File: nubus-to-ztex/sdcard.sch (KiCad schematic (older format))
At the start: 3 parts, among them J6 47219-2001

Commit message: forgot to commit last attempt at V1.2
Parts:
- J2: renamed from J6; URL (none) -> https://eu.mouser.com/ProductDetail/Molex/47219-2001?qs=6kT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
- renumbered C16 to C10
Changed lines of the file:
@@
 $Descr A4 11693 8268
 encoding utf-8
-Sheet 6 7
+Sheet 8 9
 Title "sbus-to-ztex sdcard"
 Date ""
@@
 $EndDescr
 $Comp
-L power:GND #PWR0176
+L power:GND #PWR0124
 U 1 1 58DA7C71
 P 5450 5450
-F 0 "#PWR0176" H 5450 5200 50  0001 C CNN
+F 0 "#PWR0124" H 5450 5200 50  0001 C CNN
 F 1 "GND" H 5450 5300 50  0000 C CNN
 F 2 "" H 5450 5450 50  0000 C CNN
@@
 $EndComp
 $Comp
-L power:+3V3 #PWR0177
+L power:+3V3 #PWR0125
 U 1 1 58DA7C72
 P 5450 4600
-F 0 "#PWR0177" H 5450 4450 50  0001 C CNN
+F 0 "#PWR0125" H 5450 4450 50  0001 C CNN
 F 1 "+3V3" H 5450 4740 50  0000 C CNN
 F 2 "" H 5450 4600 50  0000 C CNN
@@
 SD_D1
 $Comp
-L Device:C C16
+L Device:C C10
 U 1 1 590C7447
 P 5450 5150
-F 0 "C16" H 5475 5250 50  0000 L CNN
+F 0 "C10" H 5475 5250 50  0000 L CNN
 F 1 "47uF" H 5475 5050 50  0000 L CNN
 F 2 "Capacitor_SMD:C_0805_2012Metric" H 5488 5000 50  0001 C CNN
@@
 $EndComp
 $Comp
-L 47219-2001:47219-2001 J6
+L 47219-2001:47219-2001 J2
 U 1 1 5F6F557B
 P 4300 5250
-F 0 "J6" H 4300 5817 50  0000 C CNN
+F 0 "J2" H 4300 5817 50  0000 C CNN
 F 1 "47219-2001" H 4300 5726 50  0000 C CNN
 F 2 "MOLEX_47219-2001:MOLEX_47219-2001" H 4300 5250 50  0001 L BNN
 F 3 "https://www.molex.com/webdocs/datasheets/pdf/en-us/0472192001_MEMORY_CARD_SOCKET.pdf" H 4300 5250 50  0001 L BNN
 F 4 "47219-2001" H 4300 5250 50  0001 C CNN "MPN"
+F 5 "https://eu.mouser.com/ProductDetail/Molex/47219-2001?qs=6kT3pPPHxnVaoXw6Dd7beQ%3D%3D" H 4300 5250 50  0001 C CNN "URL"
 	1    4300 5250
 	1    0    0    -1
@@
 AR Path="/5F69F4EF/60D77AD6" Ref="C2"  Part="1"
 AR Path="/619D66B7/60D77AD6" Ref="C15"  Part="1"
-F 0 "C15" H 5225 5250 50  0000 L CNN
+AR Path="/62D70B59/60D77AD6" Ref="C9"  Part="1"
+F 0 "C9" H 5225 5250 50  0000 L CNN
 F 1 "100nF" H 5225 5050 50  0000 L CNN
 F 2 "Capacitor_SMD:C_0603_1608Metric" H 5238 5000 50  0001 C CNN

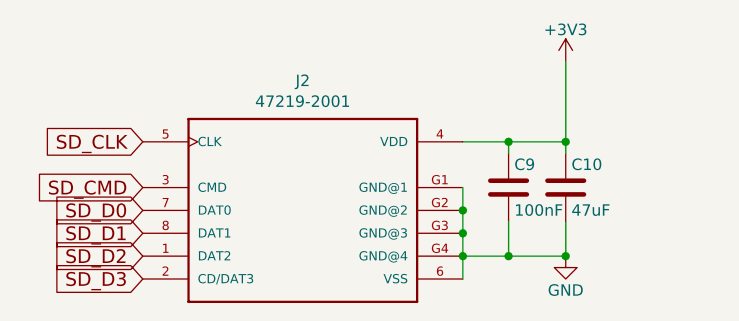
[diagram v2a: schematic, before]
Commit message: merge pmod & leds into an extended pmod on the outside. Also some BoM updates.
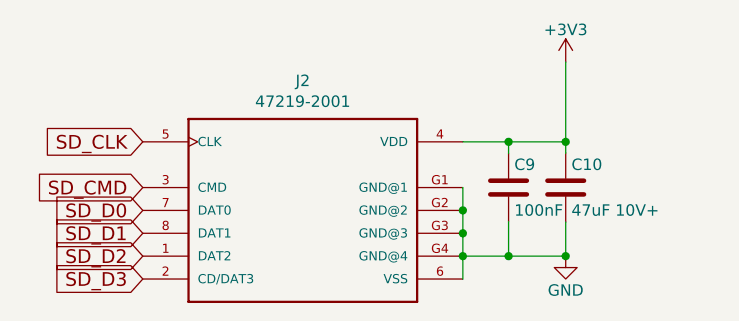
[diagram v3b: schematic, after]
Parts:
- C10: value 47uF -> 47uF 10V+; MPN GRM21BR60J476ME15L -> GRM21BR61A476ME15K; MPN-ALT (none) -> GRM21BR60J476ME15L; URL (none) -> https://www.lcsc.com/product-detail/Multilayer-Ceramic-Capa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; URL-ALT (none) -> https://www.lcsc.com/product-detail/Multilayer-Ceramic-Capa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
- C2: URL (none) -> https://lcsc.com/product-detail/Multilayer-Ceramic-Capacito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
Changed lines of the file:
@@
 $Descr A4 11693 8268
 encoding utf-8
-Sheet 8 10
+Sheet 8 9
 Title "sbus-to-ztex sdcard"
 Date ""
@@
 P 5450 5150
 F 0 "C10" H 5475 5250 50  0000 L CNN
-F 1 "47uF" H 5475 5050 50  0000 L CNN
+F 1 "47uF 10V+" H 5475 5050 50  0000 L CNN
 F 2 "Capacitor_SMD:C_0805_2012Metric" H 5488 5000 50  0001 C CNN
 F 3 "" H 5450 5150 50  0000 C CNN
-F 4 "GRM21BR60J476ME15L" H 5450 5150 50  0001 C CNN "MPN"
+F 4 "GRM21BR60J476ME15L" H 5450 5150 50  0001 C CNN "MPN-ALT"
+F 5 "https://www.lcsc.com/product-detail/Multilayer-Ceramic-Capacitors-MLCC-SMD-SMT_Murata-Electronics-GRM21BR60J476ME15L_C77072.html" H 5450 5150 50  0001 C CNN "URL-ALT"
+F 6 "GRM21BR61A476ME15K" H 5450 5150 50  0001 C CNN "MPN"
+F 7 "https://www.lcsc.com/product-detail/Multilayer-Ceramic-Capacitors-MLCC-SMD-SMT_Murata-Electronics-GRM21BR61A476ME15K_C2292827.html" H 5450 5150 50  0001 C CNN "URL"
 	1    5450 5150
 	1    0    0    -1
@@
 F 9 "?" H 5200 5150 50  0001 C CNN "Koncar"
 F 10 "TB" H 5200 5150 50  0001 C CNN "Side"
+F 11 "https://lcsc.com/product-detail/Multilayer-Ceramic-Capacitors-MLCC-SMD-SMT_YAGEO-CC0603KRX7R8BB104_C92490.html" H 3000 6050 50  0001 C CNN "URL"
 	1    5200 5150
 	1    0    0    -1

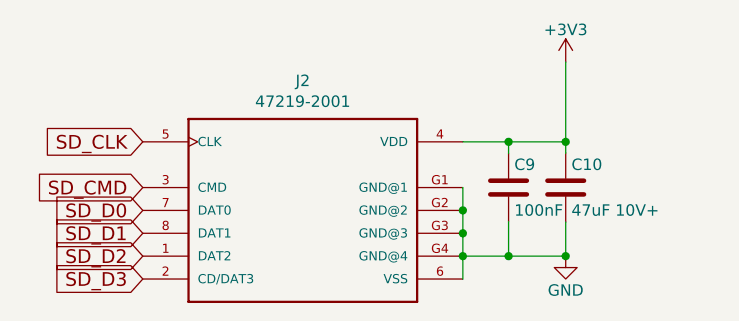
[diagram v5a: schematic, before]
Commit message: more update to V1.2 to try to limit cost
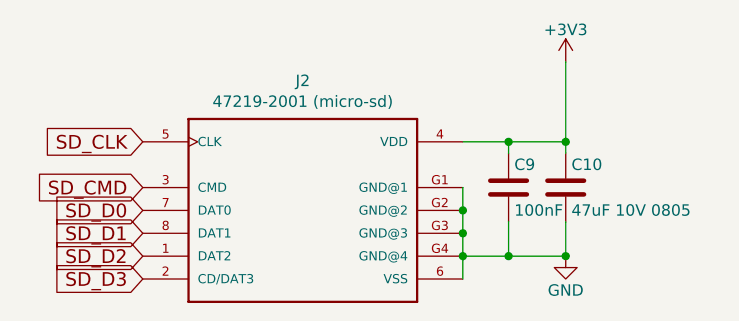
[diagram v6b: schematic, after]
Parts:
- C10: value 47uF 10V+ -> 47uF 10V 0805
- J2: value 47219-2001 -> 47219-2001 (micro-sd)
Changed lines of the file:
@@
 P 5450 5150
 F 0 "C10" H 5475 5250 50  0000 L CNN
-F 1 "47uF 10V+" H 5475 5050 50  0000 L CNN
+F 1 "47uF 10V 0805" H 5475 5050 50  0000 L CNN
 F 2 "Capacitor_SMD:C_0805_2012Metric" H 5488 5000 50  0001 C CNN
 F 3 "" H 5450 5150 50  0000 C CNN
@@
 P 4300 5250
 F 0 "J2" H 4300 5817 50  0000 C CNN
-F 1 "47219-2001" H 4300 5726 50  0000 C CNN
+F 1 "47219-2001 (micro-sd)" H 4300 5726 50  0000 C CNN
 F 2 "MOLEX_47219-2001:MOLEX_47219-2001" H 4300 5250 50  0001 L BNN
 F 3 "https://www.molex.com/webdocs/datasheets/pdf/en-us/0472192001_MEMORY_CARD_SOCKET.pdf" H 4300 5250 50  0001 L BNN

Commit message: minor cleanups
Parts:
- C2: LCSC ? -> (none)
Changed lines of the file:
@@
 F 6 "603-CC603KRX7R8BB104" H 5200 5150 50  0001 C CNN "Mouser"
 F 7 "?" H 5200 5150 50  0001 C CNN "Digikey"
-F 8 "?" H 5200 5150 50  0001 C CNN "LCSC"
+F 8 "" H 5200 5150 50  0001 C CNN "LCSC"
 F 9 "?" H 5200 5150 50  0001 C CNN "Koncar"
 F 10 "TB" H 5200 5150 50  0001 C CNN "Side"

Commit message: BoM, power plane, serial back to THT, ...
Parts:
- C10: MPN GRM21BR61A476ME15K -> C2012X5R1A476MTJ00E; URL https://www.lcsc.com/product-detail/Multilayer-Ceramic-Capacitors-MLCC-SMD-SMT_Murata-Electronics-GRM21BR61A476ME15K_C2292827.html -> https://www.lcsc.com/product-detail/Multilayer-Ceramic-Capacitors-MLCC-SMD-SMT_TDK-C2012X5R1A476MTJ00E_C76636.html
- C2: URL https://lcsc.com/product-detail/Multilayer-Ceramic-Capacito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 -> https://www.lcsc.com/product-detail/Multilayer-Ceramic-Capa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
- J2: URL https://eu.mouser.com/ProductDetail/Molex/47219-2001?qs=6kT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 -> https://www.lcsc.com/product-detail/SD-Card-Connectors_MOLE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
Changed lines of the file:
@@
 F 4 "GRM21BR60J476ME15L" H 5450 5150 50  0001 C CNN "MPN-ALT"
 F 5 "https://www.lcsc.com/product-detail/Multilayer-Ceramic-Capacitors-MLCC-SMD-SMT_Murata-Electronics-GRM21BR60J476ME15L_C77072.html" H 5450 5150 50  0001 C CNN "URL-ALT"
-F 6 "GRM21BR61A476ME15K" H 5450 5150 50  0001 C CNN "MPN"
-F 7 "https://www.lcsc.com/product-detail/Multilayer-Ceramic-Capacitors-MLCC-SMD-SMT_Murata-Electronics-GRM21BR61A476ME15K_C2292827.html" H 5450 5150 50  0001 C CNN "URL"
+F 6 "C2012X5R1A476MTJ00E" H 5450 5150 50  0001 C CNN "MPN"
+F 7 "https://www.lcsc.com/product-detail/Multilayer-Ceramic-Capacitors-MLCC-SMD-SMT_TDK-C2012X5R1A476MTJ00E_C76636.html" H 5450 5150 50  0001 C CNN "URL"
 	1    5450 5150
 	1    0    0    -1
@@
 F 3 "https://www.molex.com/webdocs/datasheets/pdf/en-us/0472192001_MEMORY_CARD_SOCKET.pdf" H 4300 5250 50  0001 L BNN
 F 4 "47219-2001" H 4300 5250 50  0001 C CNN "MPN"
-F 5 "https://eu.mouser.com/ProductDetail/Molex/47219-2001?qs=6kT3pPPHxnVaoXw6Dd7beQ%3D%3D" H 4300 5250 50  0001 C CNN "URL"
+F 5 "https://www.lcsc.com/product-detail/SD-Card-Connectors_MOLEX-472192001_C164170.html" H 4300 5250 50  0001 C CNN "URL"
 	1    4300 5250
 	1    0    0    -1
@@
 F 9 "?" H 5200 5150 50  0001 C CNN "Koncar"
 F 10 "TB" H 5200 5150 50  0001 C CNN "Side"
-F 11 "https://lcsc.com/product-detail/Multilayer-Ceramic-Capacitors-MLCC-SMD-SMT_YAGEO-CC0603KRX7R8BB104_C92490.html" H 3000 6050 50  0001 C CNN "URL"
+F 11 "https://www.lcsc.com/product-detail/Multilayer-Ceramic-Capacitors-MLCC-SMD-SMT_YAGEO-CC0603KRX7R8BB104_C92490.html" H 3000 6050 50  0001 C CNN "URL"
 	1    5200 5150
 	1    0    0    -1
